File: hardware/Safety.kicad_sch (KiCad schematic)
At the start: 9 parts, among them K1 IMB03ITS, U3 74AUP1G32

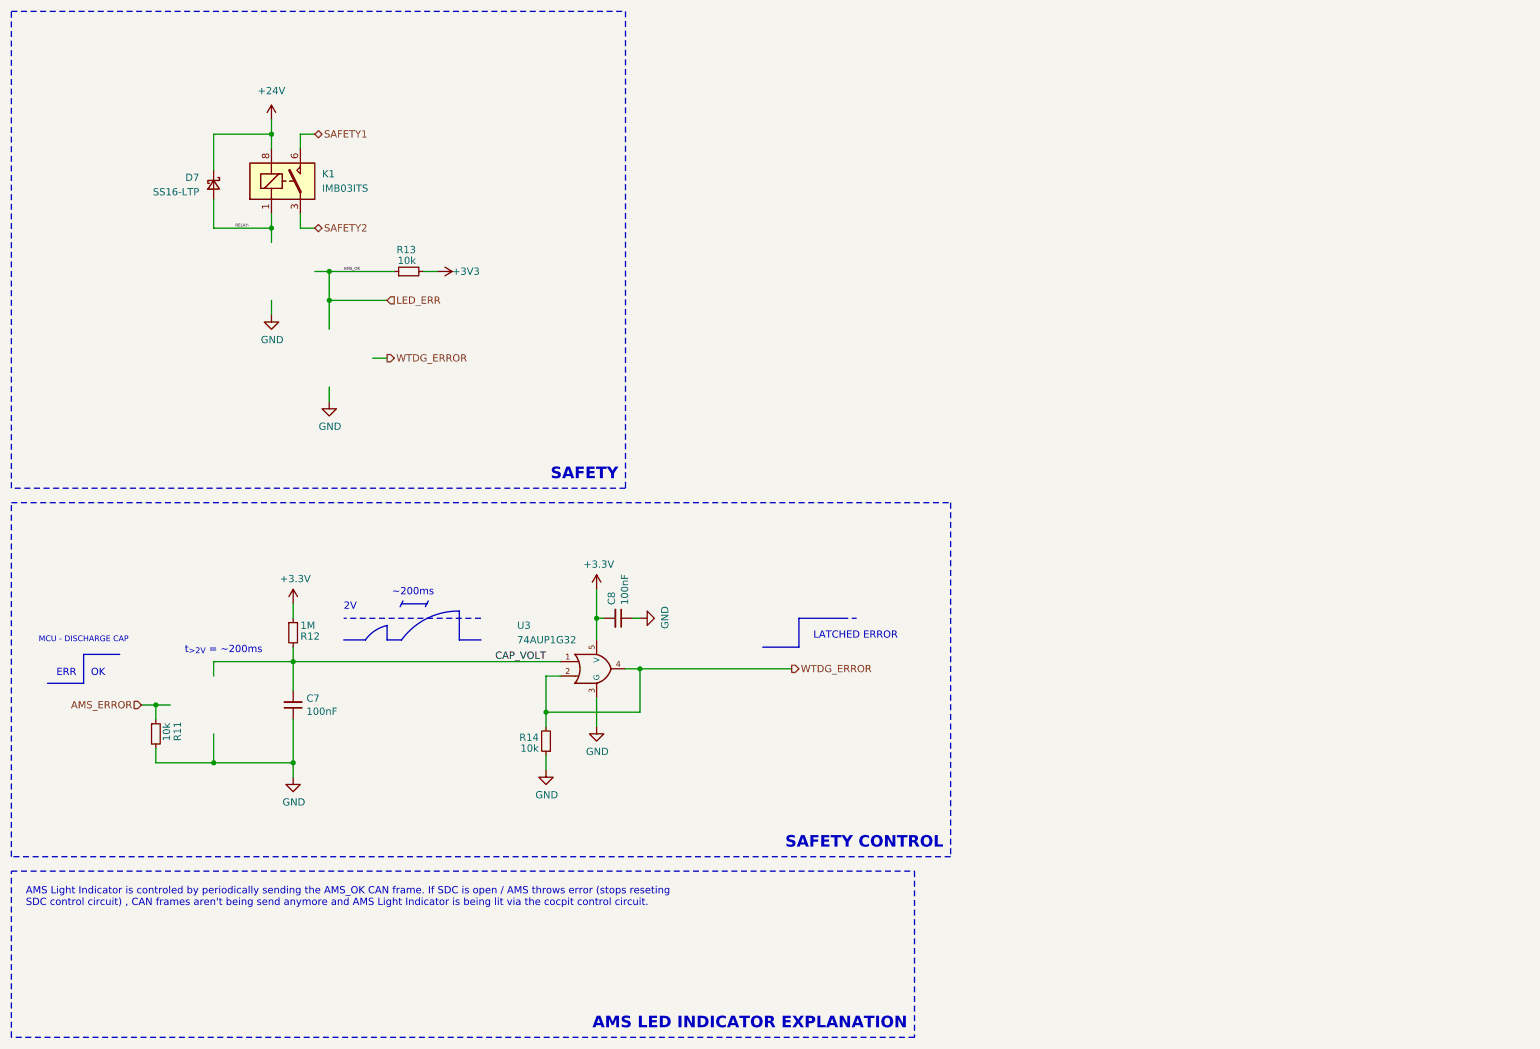
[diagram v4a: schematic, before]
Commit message: all but the communications sections done
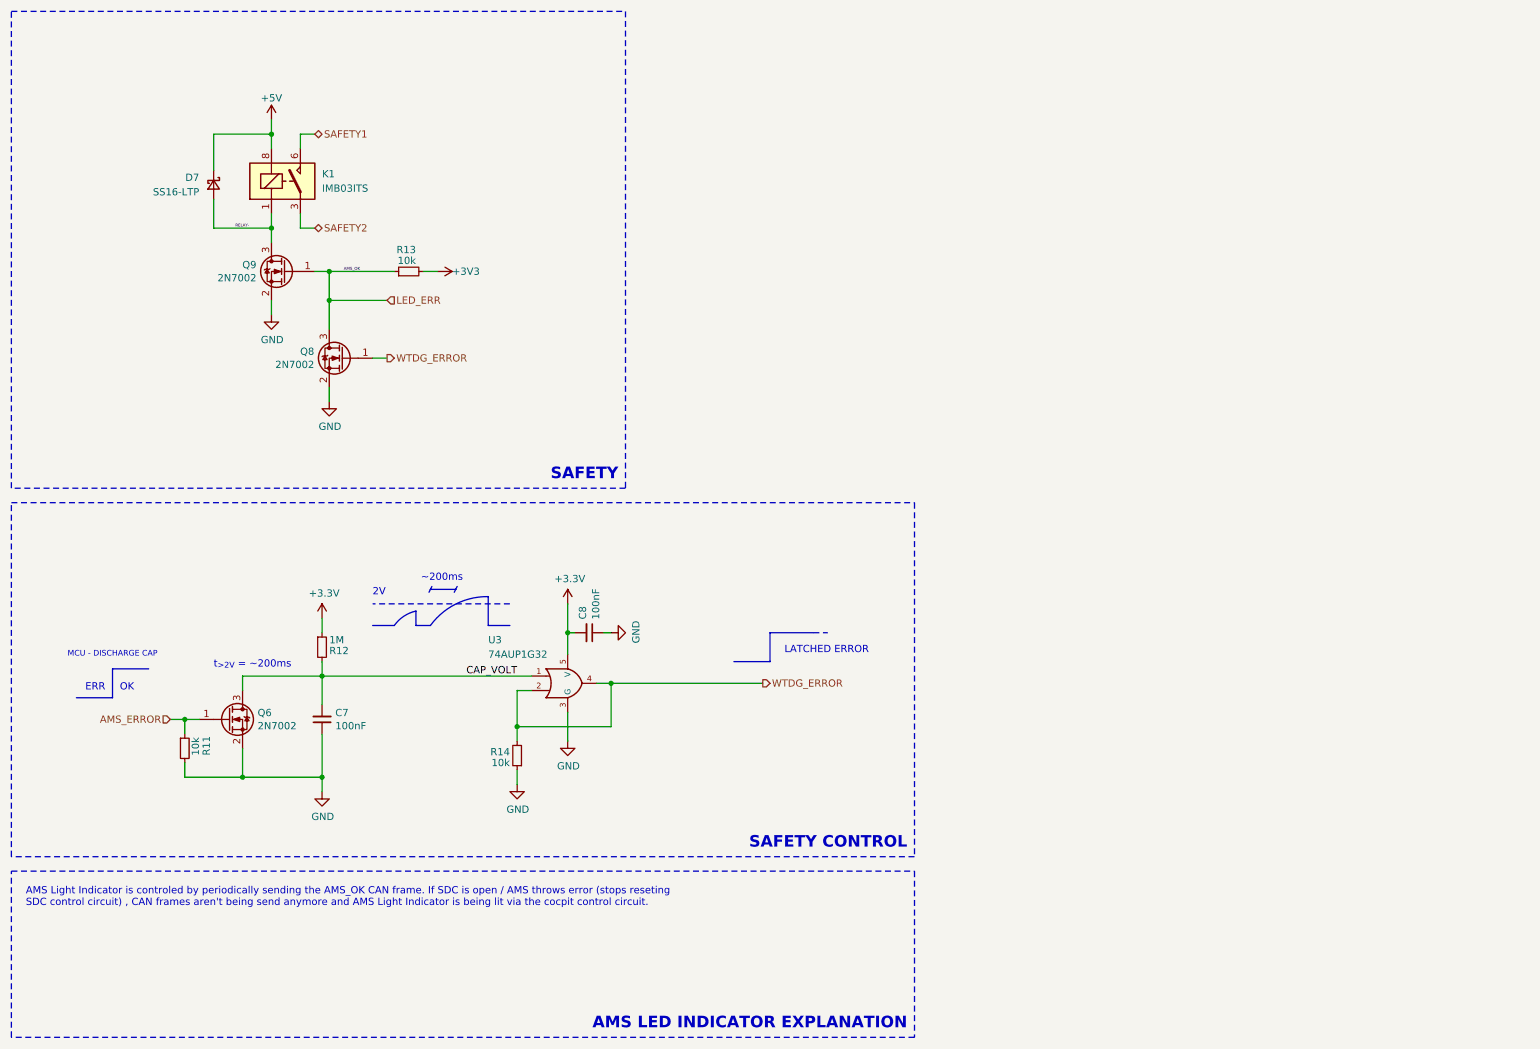
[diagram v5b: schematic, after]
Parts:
- added Q6, Q8, Q9: 2N7002, Package_TO_SOT_SMD:SOT-23, symbol Transistor_FET:2N7002
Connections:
- net AMS_ERROR: now also Q6.1 (G)
- net CAP_VOLT: now also Q6.3 (D)
- net GND: now also Q6.2 (S), Q8.2 (S), Q9.2 (S)
- net LED_ERR: now also Q8.3 (D), Q9.1 (G)
- net RELAY-: now also Q9.3 (D)
- net WTDG_ERROR: now also Q8.1 (G)
- net +24V renamed +5V
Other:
- moved on the sheet: C7, C8, R11, R12, R14, U3

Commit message: sync
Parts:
- added R100: 100, Resistor_SMD:R_0603_1608Metric, symbol Device:R_Small
- C7, C8: Mouser Price/Stock (none) -> https://www.mouser.pl/ProductDetail/KEMET/C0603C104J3RACTU?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
- R11, R13, R14: Mouser Price/Stock (none) -> https://www.mouser.pl/ProductDetail/YAGEO/RT0603DRE07100KL?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
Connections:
- net AMS_ERROR: now also R100.1; no longer Q6.1 (G), R11.1
- new net: Q6.1 (G), R100.2, R11.1
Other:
- moved on the sheet: C7, C8, Q6, R11, R12, R14, U3

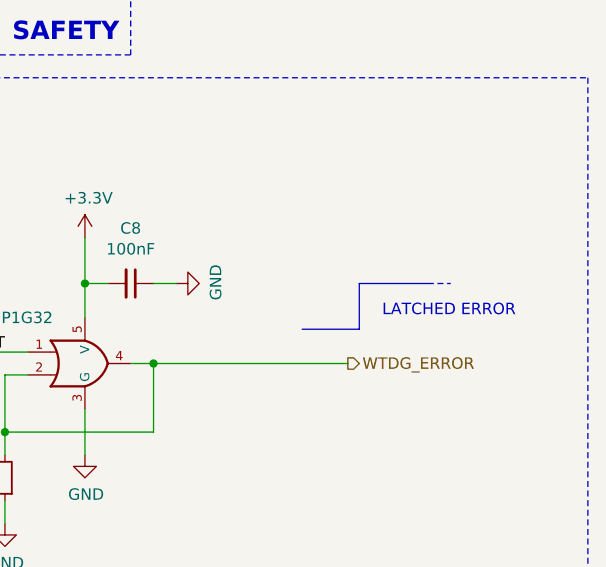
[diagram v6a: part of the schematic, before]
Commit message: the connectors wil stay and wont be changed further
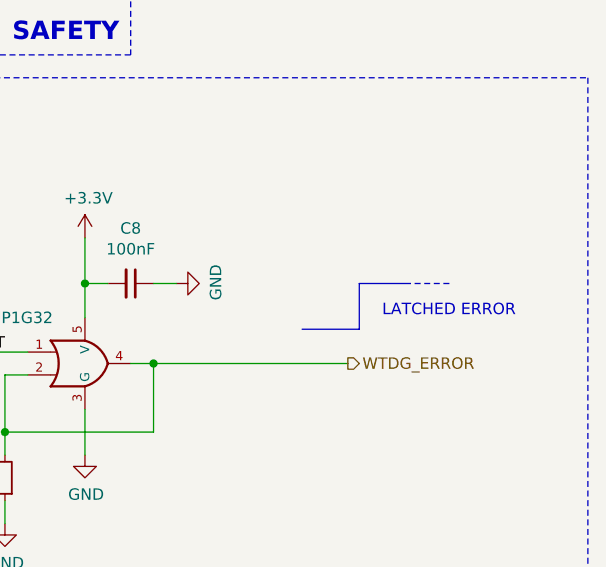
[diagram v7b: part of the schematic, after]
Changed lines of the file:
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@@
 			(width 0)
 			(type default)
-		)
-	)
-	(polyline
-		(pts
-			(xy 156.21 124.46) (xy 148.59 124.46)
-		)
-		(stroke
-			(width 0)
-			(type default)
+			(color 132 0 132 1)
+		)
+	)
+	(polyline
+		(pts
+			(xy 153.67 124.46) (xy 148.59 124.46)
+		)
+		(stroke
+			(width 0)
+			(type default)
+			(color 132 0 132 1)
 		)
 	)
@@
 			(width 0)
 			(type default)
+			(color 132 0 132 1)
 		)
 	)
@@
 			(width 0)
 			(type default)
+			(color 132 0 132 1)
 		)
 	)
@@
 			(width 0)
 			(type default)
+			(color 132 0 132 1)
 		)
 	)
@@
 			(width 0)
 			(type default)
+			(color 132 0 132 1)
 		)
 	)
@@
 			(width 0)
 			(type default)
+			(color 132 0 132 1)
 		)
 	)
@@
 			(width 0)
 			(type default)
+			(color 132 0 132 1)
 		)
 	)
@@
 			(width 0)
 			(type default)
-		)
-	)
-	(polyline
-		(pts
-			(xy 156.21 124.46) (xy 158.75 124.46)
-		)
-		(stroke
-			(width 0)
-			(type dot)
+			(color 132 0 132 1)
+		)
+	)
+	(polyline
+		(pts
+			(xy 153.67 124.46) (xy 158.75 124.46)
+		)
+		(stroke
+			(width 0)
+			(type dash)
+			(color 132 0 132 1)
 		)
 	)
@@
 			(width 0)
 			(type default)
+			(color 132 0 132 1)
 		)
 	)
@@
 			(width 0)
 			(type dash)
+			(color 132 0 132 1)
 		)
 	)
@@
 			(width 0)
 			(type default)
+			(color 132 0 132 1)
 		)
 	)
@@
 			(width 0)
 			(type default)
+			(color 132 0 132 1)
 		)
 	)
@@
 			(width 0)
 			(type default)
+			(color 132 0 132 1)
 		)
 	)
@@
 			(width 0)
 			(type default)
+			(color 132 0 132 1)
 		)
 	)
@@
 			(width 0)
 			(type default)
+			(color 132 0 132 1)
 		)
 	)
@@
 			(width 0)
 			(type default)
+			(color 132 0 132 1)
 		)
 	)
@@
 			(width 0)
 			(type default)
+			(color 132 0 132 1)
 		)
 		(fill
@@
 			(width 0)
 			(type default)
+			(color 132 0 132 1)
 		)
 		(fill
@@
 			(font
 				(size 1 1)
+				(color 132 0 132 1)
 			)
 		)
@@
 			(font
 				(size 1.27 1.27)
+				(color 132 0 132 1)
 			)
 			(justify top)
@@
 			(font
 				(size 1.27 1.27)
+				(color 132 0 132 1)
 			)
 			(justify left bottom)
@@
 			(font
 				(size 1.27 1.27)
+				(color 132 0 132 1)
 			)
 			(justify right bottom)
@@
 			(font
 				(size 1.27 1.27)
+				(color 132 0 132 1)
 			)
 			(justify right top)
@@
 			(font
 				(size 1.27 1.27)
+				(color 132 0 132 1)
 			)
 			(justify left bottom)
@@
 			(font
 				(size 1.27 1.27)
+				(color 132 0 132 1)
 			)
 			(justify left bottom)
@@
 			(font
 				(size 1.27 1.27)
+				(color 132 0 132 1)
 			)
 			(justify left bottom)

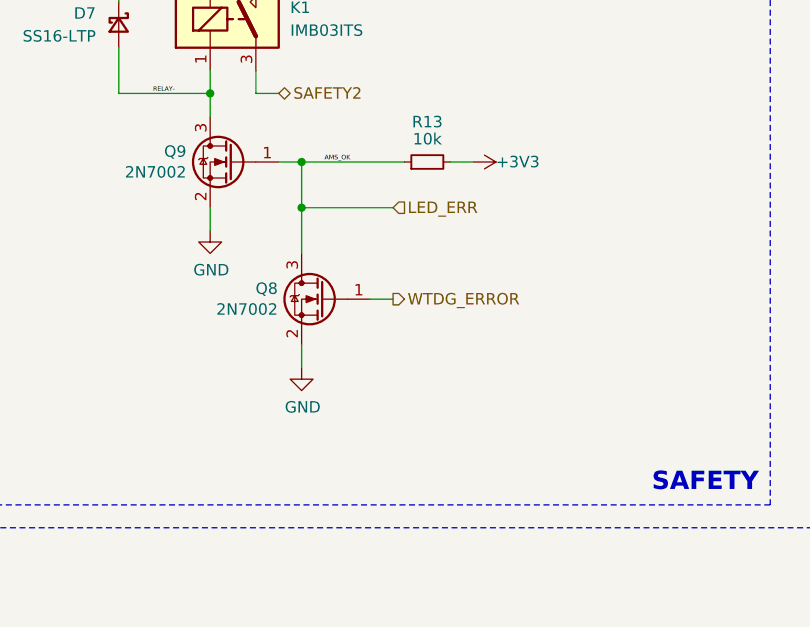
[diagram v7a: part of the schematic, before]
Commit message: LV section component placement done
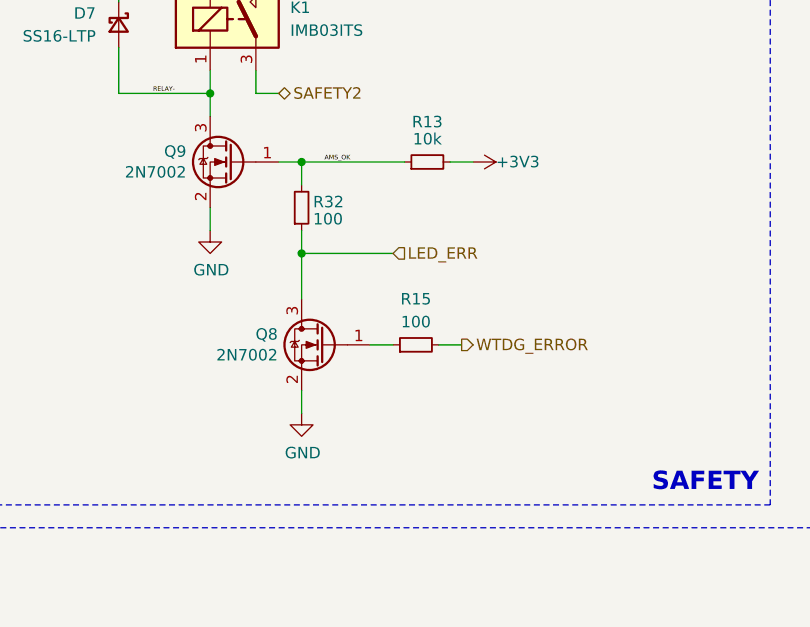
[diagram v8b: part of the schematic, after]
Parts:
- added R15, R32: 100, Resistor_SMD:R_0603_1608Metric, symbol Device:R_Small
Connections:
- net LED_ERR: now also R32.1; no longer Q9.1 (G), R13.1
- net WTDG_ERROR: now also R15.2; no longer Q8.1 (G)
- new net: Q8.1 (G), R15.1
- new net AMS_OK: Q9.1 (G), R13.1, R32.2
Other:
- moved on the sheet: Q8
